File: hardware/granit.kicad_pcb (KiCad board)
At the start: 4 copper layers, 92 x 100 mm, 108 parts, among them IC1 ASM1061, J1 12V Barrel, J2 12V Screw Terminal, J3 RJ45_RB1-125B8G1A, J6 Conn_01x02, J7 USB_C_Receptacle_USB2.0_14P, J8 Conn_01x03, J9 SATA_22pin, Q1 FDS4435BZ, Q2 FDS4435BZ, Q3 FDS4435BZ, Q4 2N7002, Q5 2N7002, Q6 2N7002, SW1 SW_Push, U1 NCP1117-3.3_SOT223, U2 AP64501SP-13, U3 74AHCT1G125, U4 DS3231MZ, U5 USBLC6-2SC6, U6 74AHCT1G32, Y1 Crystal

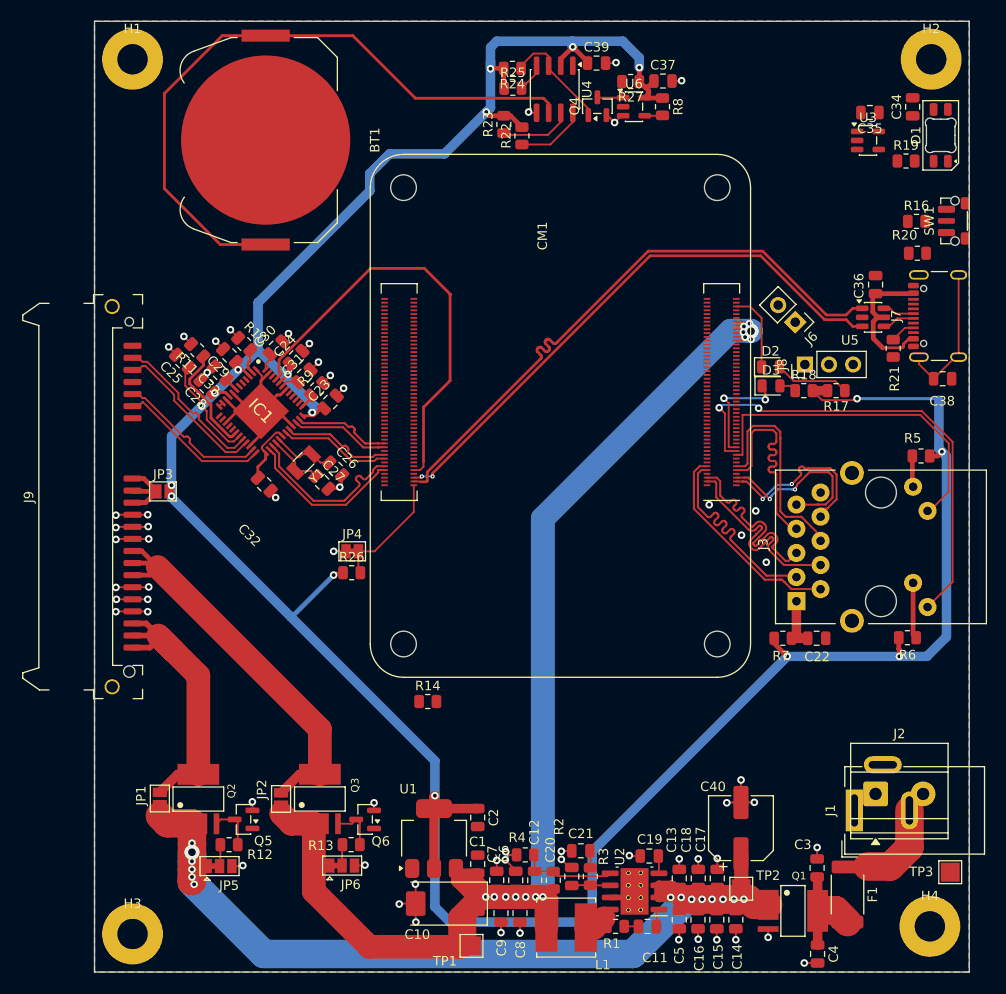
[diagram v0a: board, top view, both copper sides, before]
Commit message: Clean up silkscreen labels
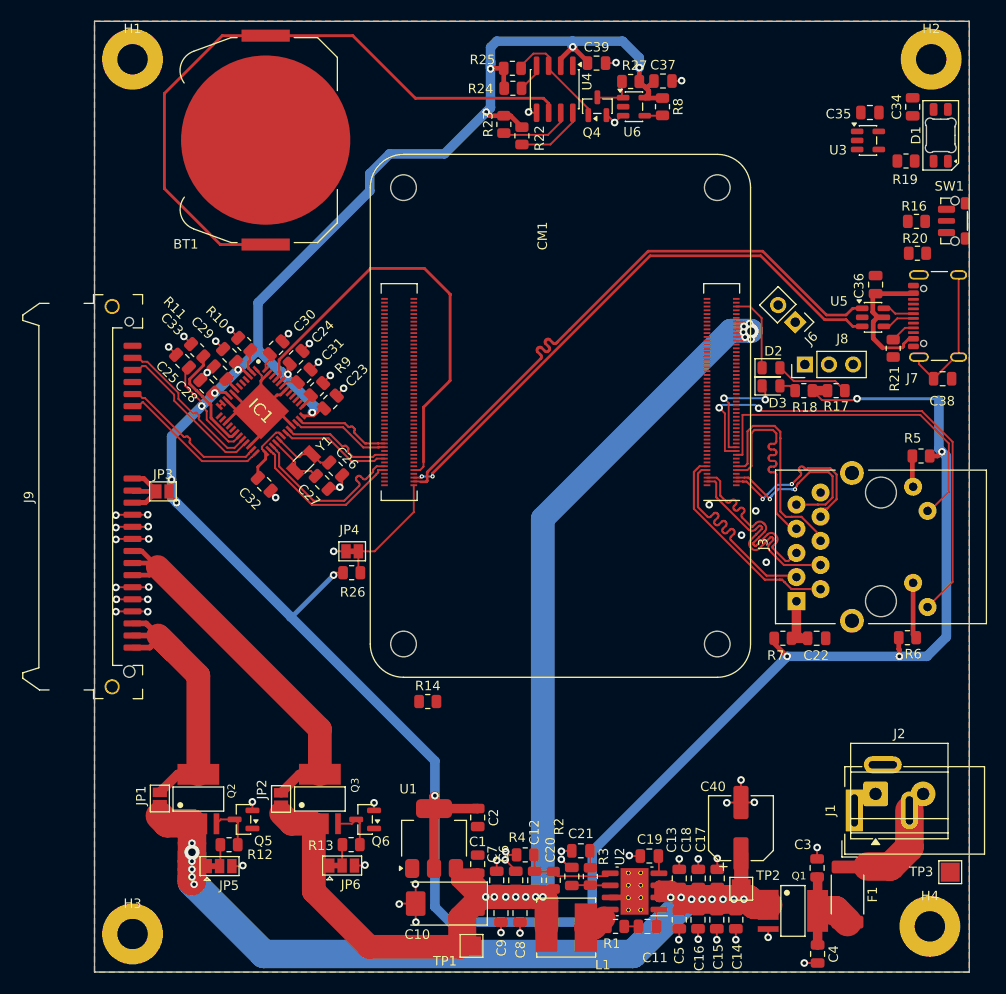
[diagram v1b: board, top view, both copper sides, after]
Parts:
- moved D2 0.11 mm to (91.2, 56.5)
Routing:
- net +3V3: track 326.1 -> 327.6 mm

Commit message: Change NeoPixel D1 to WS2812B 5mm SMD (PLCC4)
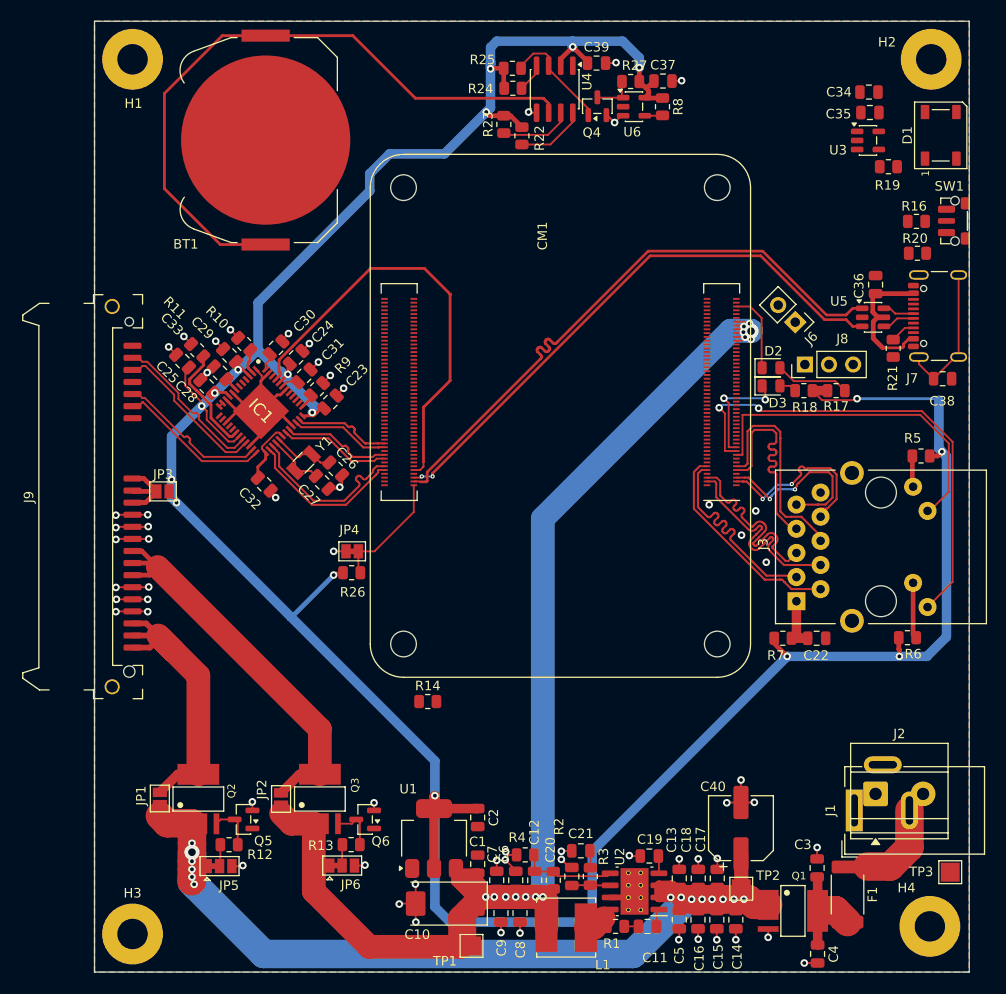
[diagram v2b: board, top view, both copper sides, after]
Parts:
- D1: value SK6812MINI-E -> WS2812B-5mm; footprint LED_SMD:LED_SK6812MINI-E_3.2x2.8mm_P1.5mm_ReverseMount -> LED_SMD:LED_WS2812B_PLCC4_5.0x5.0mm_P3.2mm
- moved C34 4.85 mm to (101.5, 27.4), turned to 180 degrees
- moved R19 1.94 mm to (103.5, 35.3)

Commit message: Move RTC south of CM4, avoid USB crossing
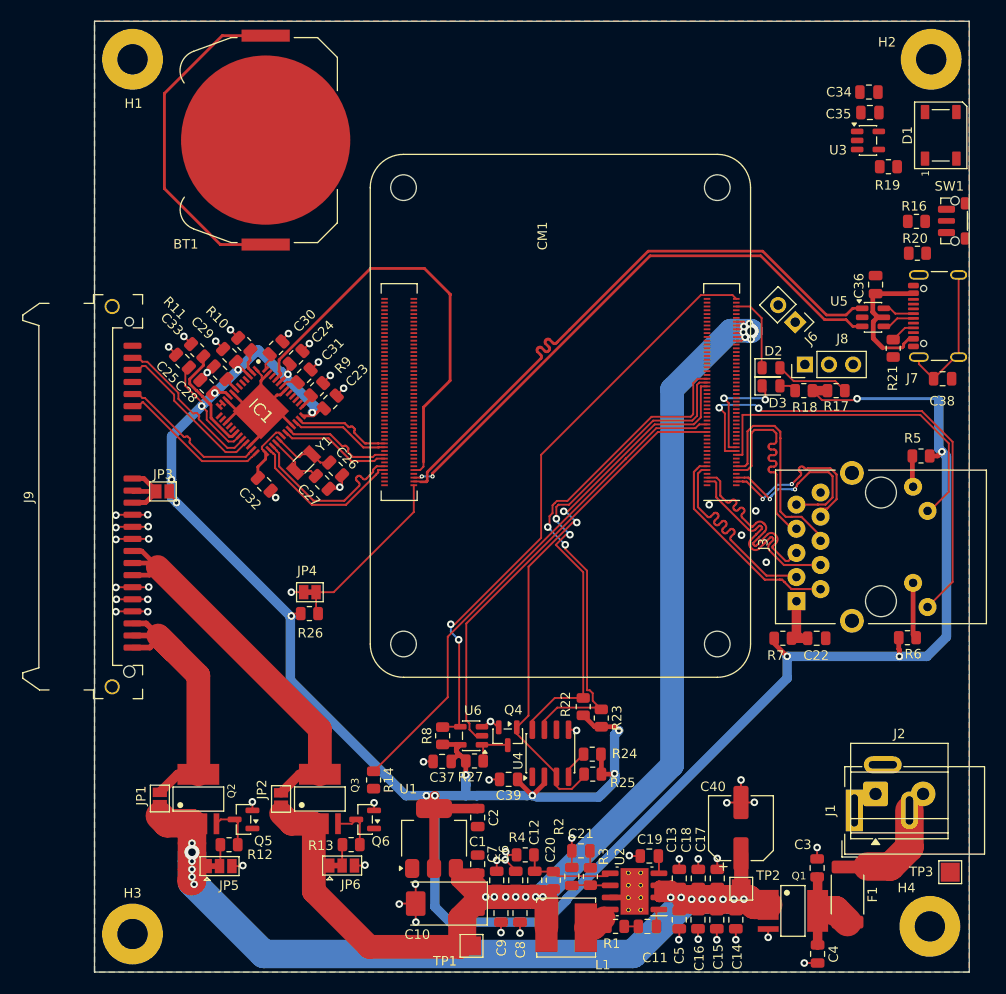
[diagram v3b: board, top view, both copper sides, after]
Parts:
- moved C39 75.9 mm to (63.6, 99.7), turned to 180 degrees
- moved C37 75.2 mm to (56.6, 97.8), turned to 180 degrees
- moved R24 74.7 mm to (72.4, 99.2), turned to 0 degrees
- moved R27 73.3 mm to (60.0, 97.8), turned to 0 degrees
- moved R25 70.5 mm to (72.4, 97.1), turned to 180 degrees
- moved R8 70.1 mm to (56.6, 95.1), turned to 90 degrees
- moved U4 69.8 mm to (68.0, 97.0), turned to 90 degrees
- moved U6 68.3 mm to (59.6, 95.1), turned to 180 degrees
- moved Q4 66.9 mm to (63.5, 95.2), turned to -90 degrees
- moved R23 63.3 mm to (73.3, 93.3), turned to -90 degrees
- moved R22 60.4 mm to (71.4, 92.1), turned to -90 degrees
- moved R14 10.0 mm to (49.4, 99.8), turned to 90 degrees
- moved JP4 6.19 mm to (42.6, 80.0)
- moved R26 6.19 mm to (42.6, 82.3)
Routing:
- net GLOBAL_EN: track 1.88 -> 63.4 mm, vias 0 -> 2
- net SATA_PWR_EN: track 0.00 -> 54.1 mm
- net RTC_INT: track 11.7 -> 60.4 mm, vias 0 -> 2
- net SDA1: track 7.60 -> 56.0 mm, vias 0 -> 2
- net GPIO_HOLD: track 0.00 -> 46.6 mm
- net SCL1: track 7.31 -> 53.2 mm, vias 0 -> 2
- net +3V3: track 327.6 -> 285.0 mm, vias 17 -> 18
- net Net-(BT1-+): track 70.0 -> 36.3 mm
- net USB_OTG_ID: track 12.7 -> 18.9 mm
- net GND: track 107.2 -> 107.8 mm, vias 61 -> 60

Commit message: Add GND vias to CM4 connector pads
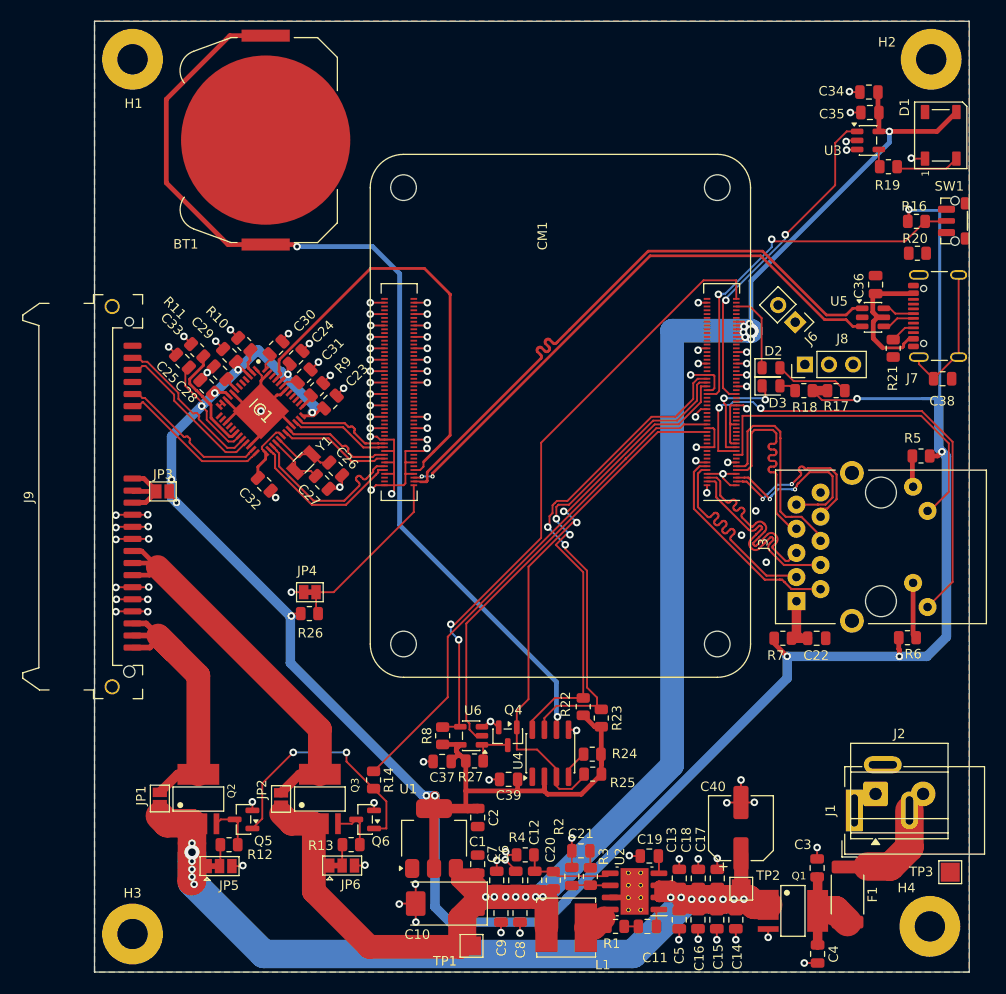
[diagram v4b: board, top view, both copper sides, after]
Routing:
- net GND: track 107.8 -> 203.8 mm, vias 60 -> 107
- net Net-(BT1-+): track 36.3 -> 105.4 mm, vias 0 -> 2
- net +5VP: track 154.4 -> 198.2 mm, vias 13 -> 14
- net BUTTON: track 0.00 -> 39.6 mm, vias 0 -> 2
- net NEOPIXEL: track 0.00 -> 35.1 mm, vias 0 -> 2
- net Net-(Q5-G): track 0.00 -> 26.4 mm, vias 0 -> 2
- net +3V3: track 285.0 -> 299.0 mm, vias 18 -> 15
- net Net-(D1-DIN): track 0.00 -> 6.76 mm
- net GLOBAL_EN: track 63.4 -> 66.5 mm
- net Net-(R19-Pad1): track 0.00 -> 1.85 mm
- net SCL1: track 53.2 -> 52.3 mm
- net ETH_nLED1: track 50.7 -> 51.6 mm
- net SDA1: track 56.0 -> 55.2 mm

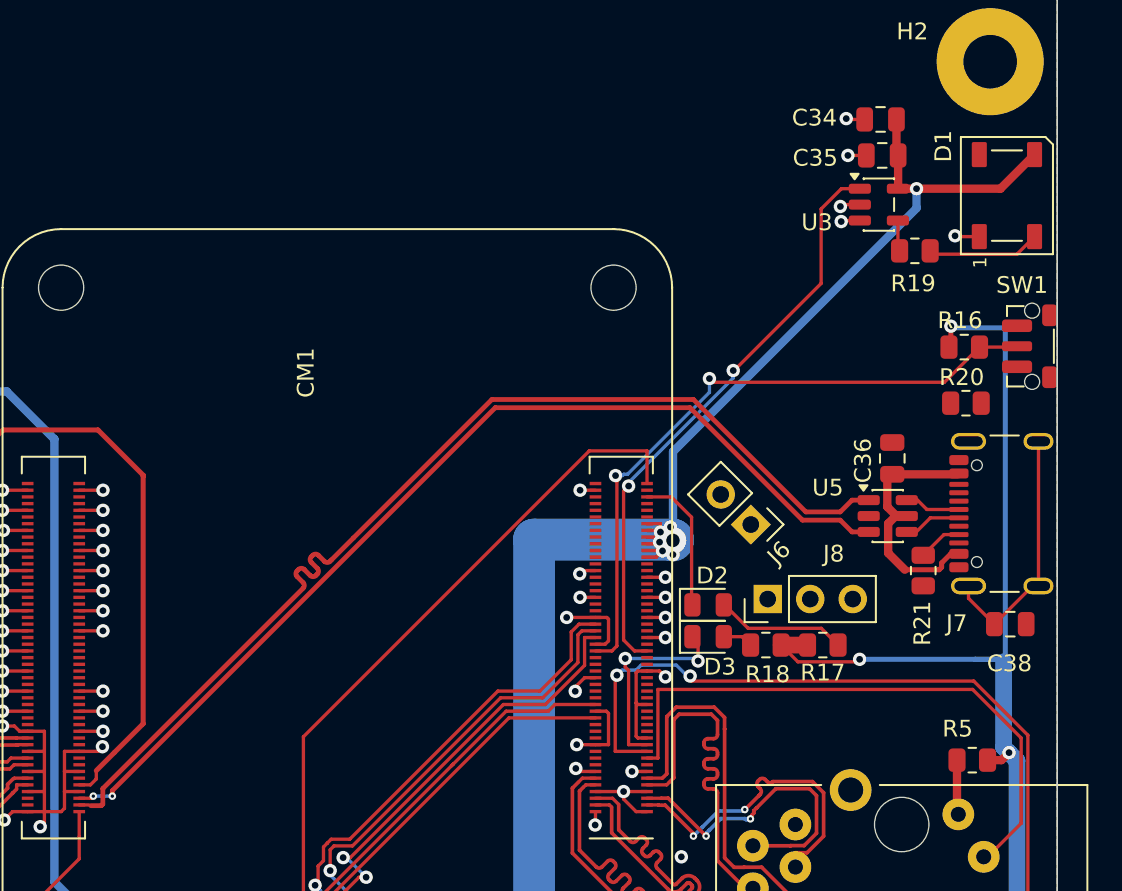
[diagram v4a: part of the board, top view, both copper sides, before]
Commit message: Move USB-C connector north, improve routing
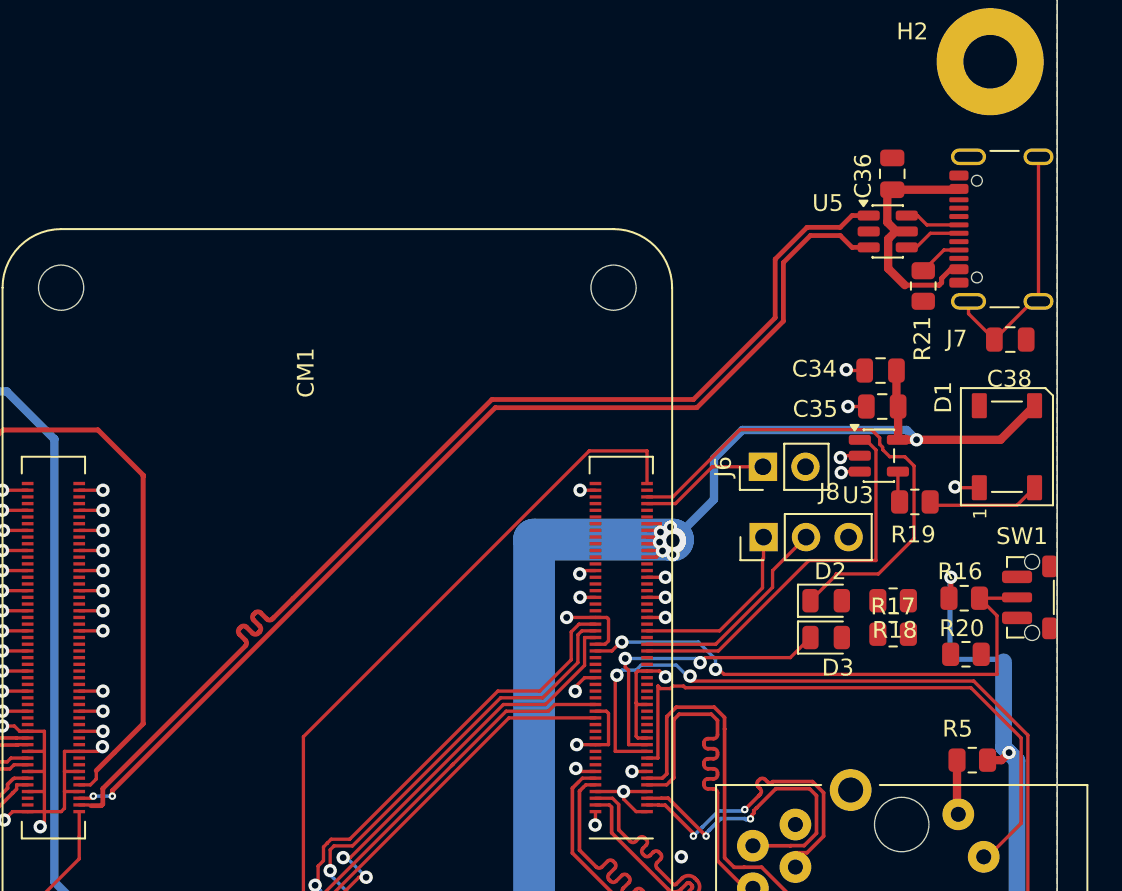
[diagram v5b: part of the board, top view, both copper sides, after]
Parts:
- moved C36 17.0 mm to (102.2, 30.7)
- moved C38 17.0 mm to (109.2, 40.6)
- moved J7 17.0 mm to (109.8, 34.0)
- moved R21 17.0 mm to (104.0, 37.4)
- moved U5 17.0 mm to (101.9, 34.1)
- moved C34 15.0 mm to (101.5, 42.5)
- moved C35 15.0 mm to (101.5, 44.6)
- moved D1 15.0 mm to (109.0, 47.0)
- moved R16 15.0 mm to (106.5, 56.0)
- moved R19 15.0 mm to (103.5, 50.3)
- moved R20 15.0 mm to (106.5, 59.4)
- moved SW1 15.0 mm to (110.5, 56.0)
- moved U3 15.0 mm to (101.3, 47.5)
- moved R18 8.05 mm to (102.2, 56.2)
- moved D2 7.05 mm to (98.2, 56.2)
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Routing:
- net +3V3: track 299.0 -> 268.8 mm, vias 15 -> 14
- net nLED_PWR: track 8.30 -> 30.9 mm
- net UART_RX: track 0.00 -> 12.7 mm
- net NEOPIXEL: track 35.1 -> 23.7 mm, vias 2 -> 0
- net UART_TX: track 0.00 -> 11.0 mm
- net +5VP: track 198.2 -> 190.1 mm
- net Net-(D2-A): track 7.98 -> 0.00 mm
- net nRPIBOOT: track 0.00 -> 7.84 mm
- net BUTTON: track 39.6 -> 32.6 mm
- net nLED_ACT: track 12.3 -> 18.1 mm
- net USB_DN: track 63.8 -> 67.3 mm
- net USB_DP: track 60.1 -> 63.6 mm
- net Net-(D3-A): track 1.81 -> 0.00 mm
- net GND: track 203.8 -> 202.7 mm, vias 107 -> 106

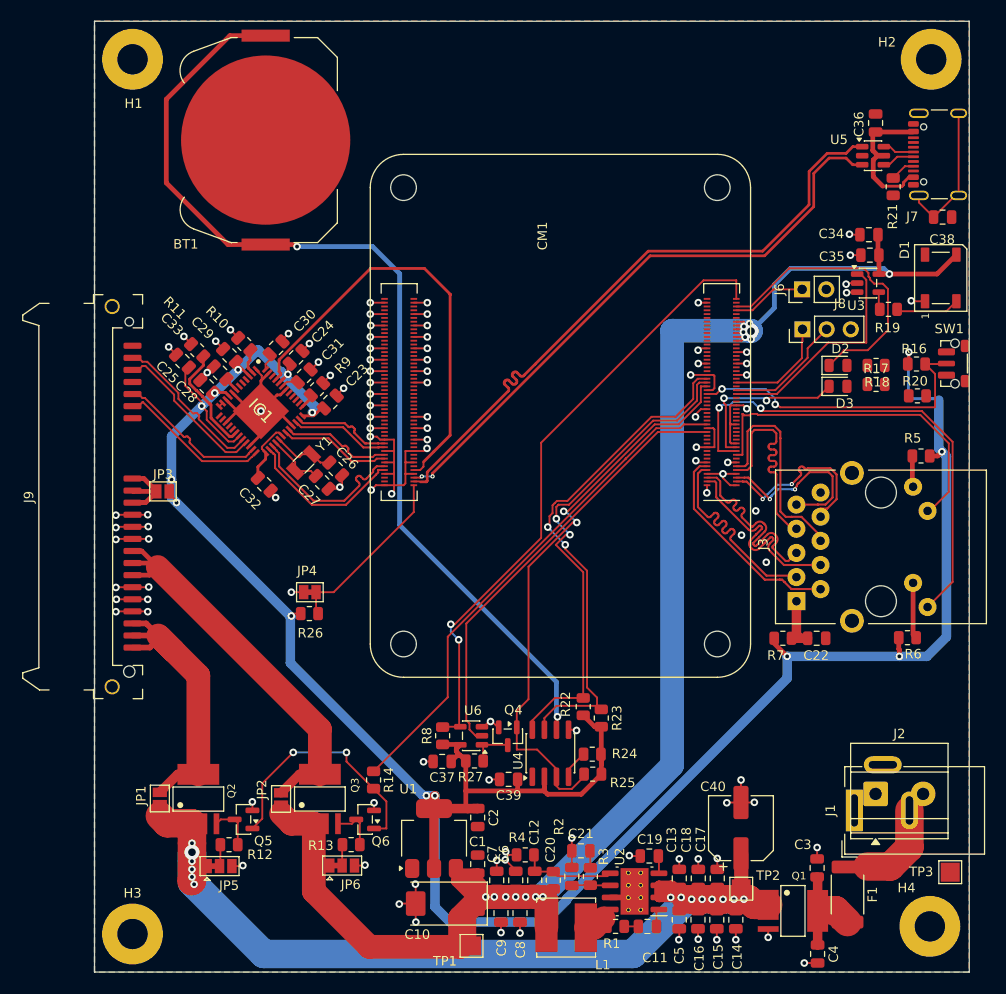
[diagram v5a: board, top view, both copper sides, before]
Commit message: Adjust trace routing
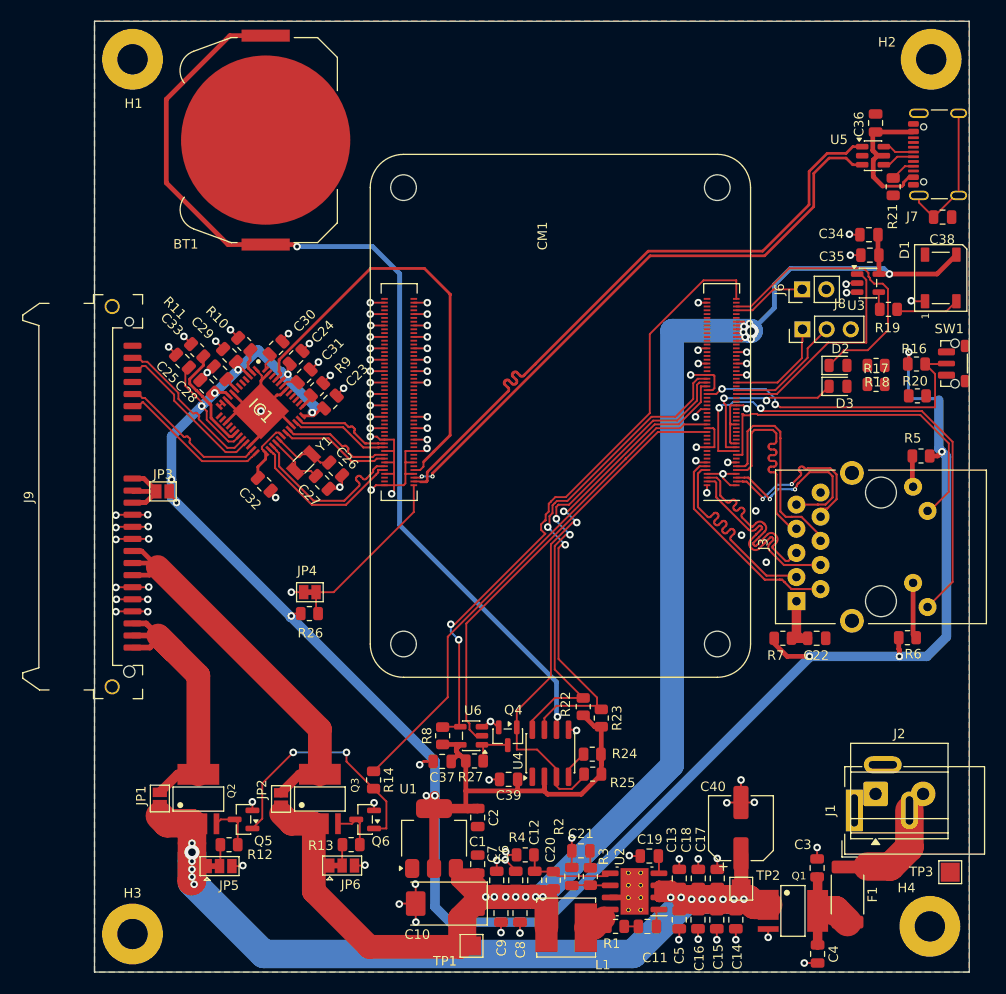
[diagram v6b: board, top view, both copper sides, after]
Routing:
- net GLOBAL_EN: track 66.5 -> 67.6 mm
- net GND: track 202.7 -> 203.7 mm
- net SDA1: track 55.2 -> 56.0 mm

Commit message: Routing optimisations, add fiducial markers
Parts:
- removed R20: 5K1, Resistor_SMD:R_0805_2012Metric
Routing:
- net BUTTON: track 32.6 -> 28.2 mm
- net +3V3: track 269.1 -> 266.0 mm
